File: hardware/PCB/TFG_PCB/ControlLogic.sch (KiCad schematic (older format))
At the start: 2 parts, among them J31 Raspberry_Pi_2_3, U7 CD74HC4067M

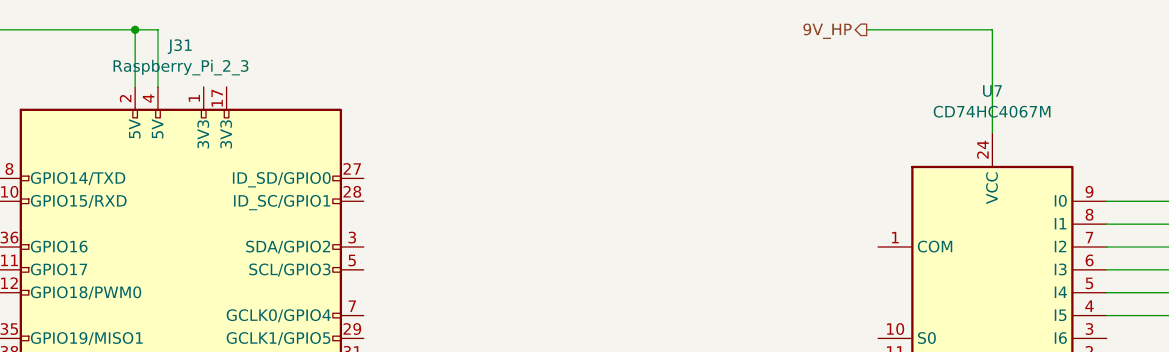
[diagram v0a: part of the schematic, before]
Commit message: added footprints
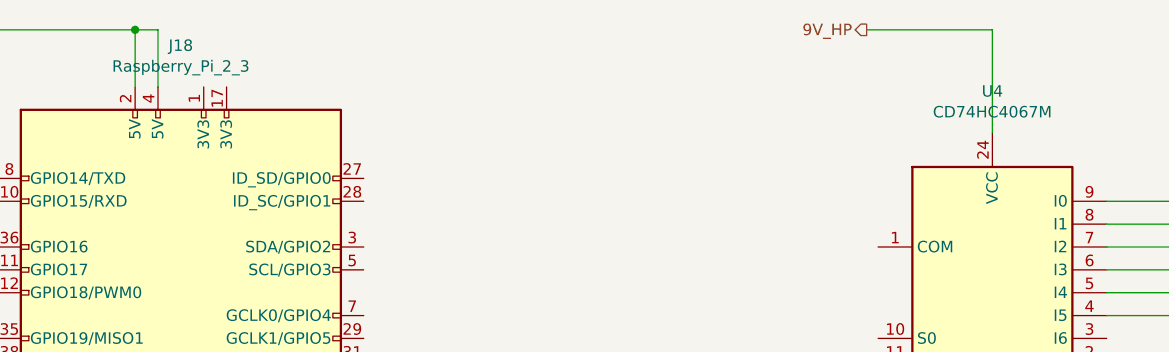
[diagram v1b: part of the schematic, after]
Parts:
- renumbered J31 to J18, U7 to U4
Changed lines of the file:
@@
 $EndDescr
 $Comp
-L Connector:Raspberry_Pi_2_3 J31
+L Connector:Raspberry_Pi_2_3 J18
 U 1 1 5E97206E
 P 3700 3450
-F 0 "J31" H 3700 4931 50  0000 C CNN
+F 0 "J18" H 3700 4931 50  0000 C CNN
 F 1 "Raspberry_Pi_2_3" H 3700 4840 50  0000 C CNN
 F 2 "" H 3700 3450 50  0001 C CNN
@@
 Connection ~ 3500 1900
 $Comp
-L 74xx:CD74HC4067M U7
+L 74xx:CD74HC4067M U4
 U 1 1 5E9A928D
 P 7250 3350
-F 0 "U7" H 7250 4531 50  0000 C CNN
+F 0 "U4" H 7250 4531 50  0000 C CNN
 F 1 "CD74HC4067M" H 7250 4440 50  0000 C CNN
 F 2 "Package_SO:SOIC-24W_7.5x15.4mm_P1.27mm" H 8150 2350 50  0001 C CIN
@@
 	3400 4850 3500 4850
 $Comp
-L power:GND #PWR0141
+L power:GND #PWR041
 U 1 1 5E9AD34B
 P 3650 4850
-F 0 "#PWR0141" H 3650 4600 50  0001 C CNN
+F 0 "#PWR041" H 3650 4600 50  0001 C CNN
 F 1 "GND" H 3655 4677 50  0000 C CNN
 F 2 "" H 3650 4850 50  0001 C CNN

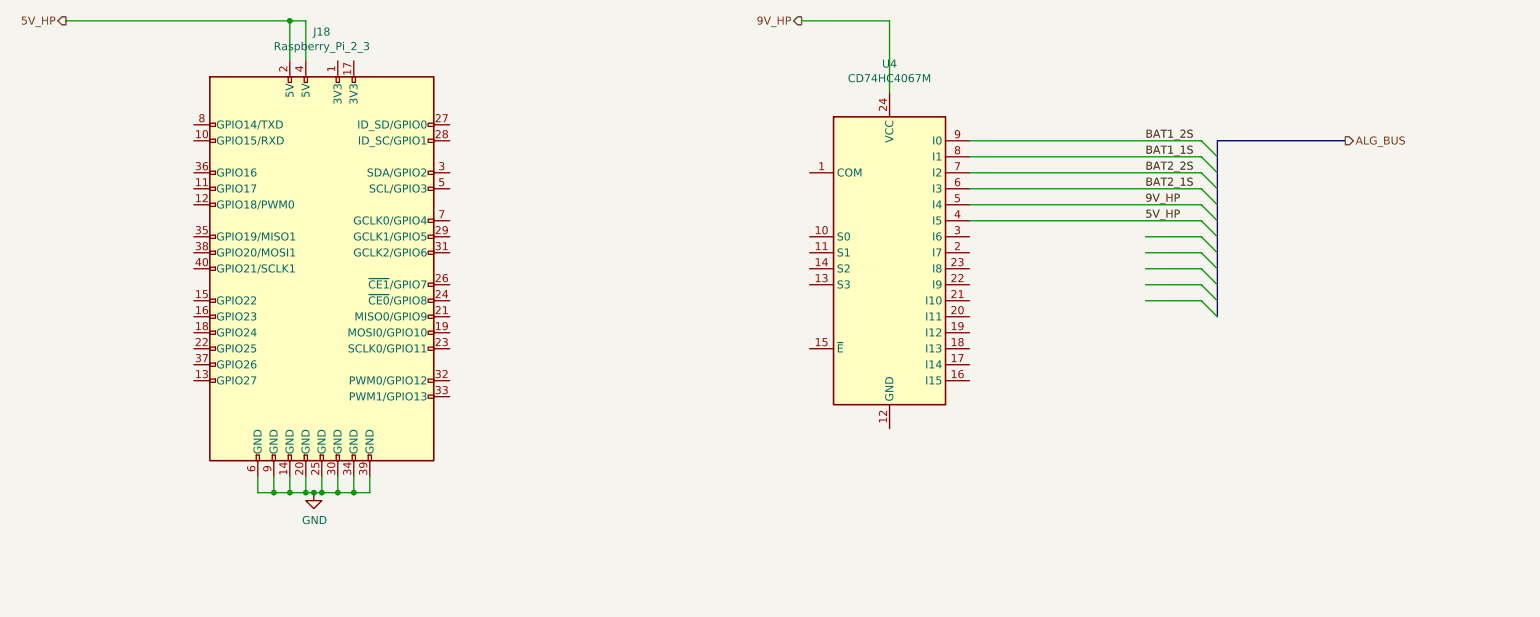
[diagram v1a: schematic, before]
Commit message: netlist and Motor Control sheet
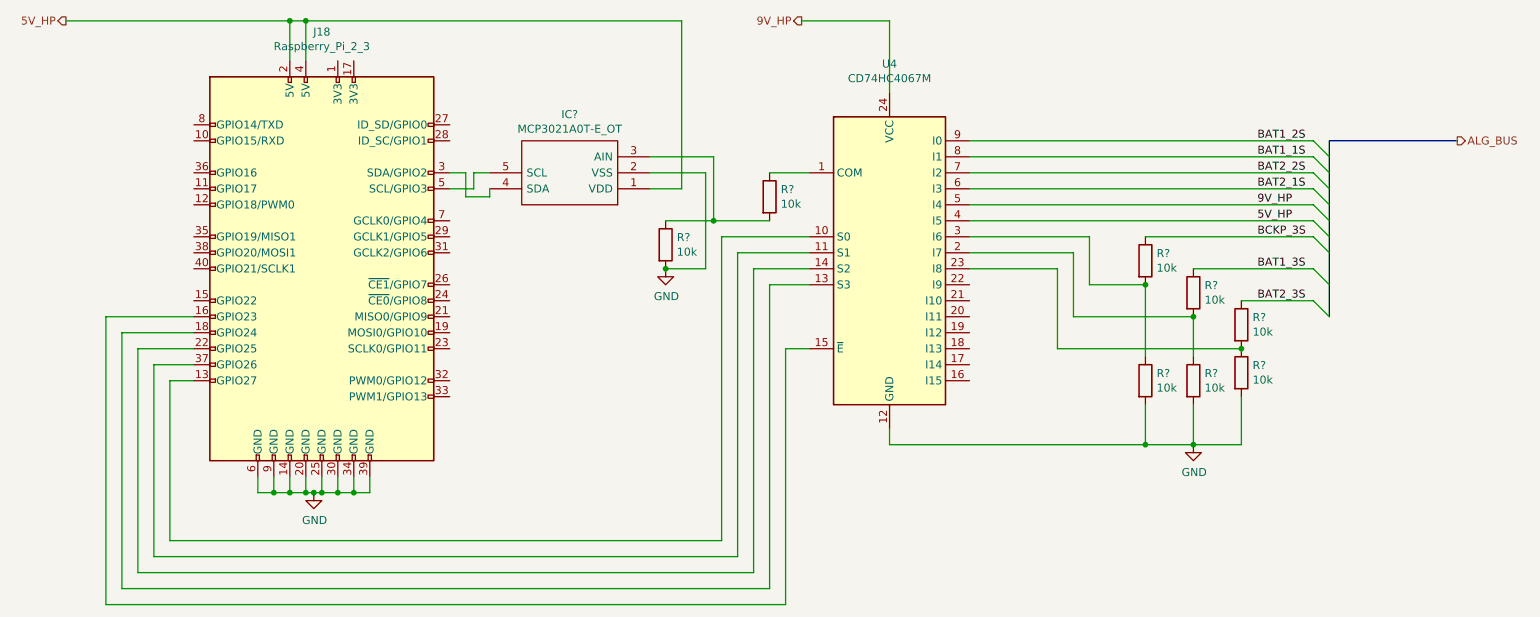
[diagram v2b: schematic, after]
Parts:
- added IC?: MCP3021A0T-E_OT, SOT95P280X145-5N, symbol SamacSys_Parts:MCP3021A0T-E_OT
- added R? (x8): 10k, symbol Device:R
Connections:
- net labels added: BAT1_3S, BAT2_3S, BCKP_3S
- wire segments 33 -> 92

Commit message: Updated netlist and footprints
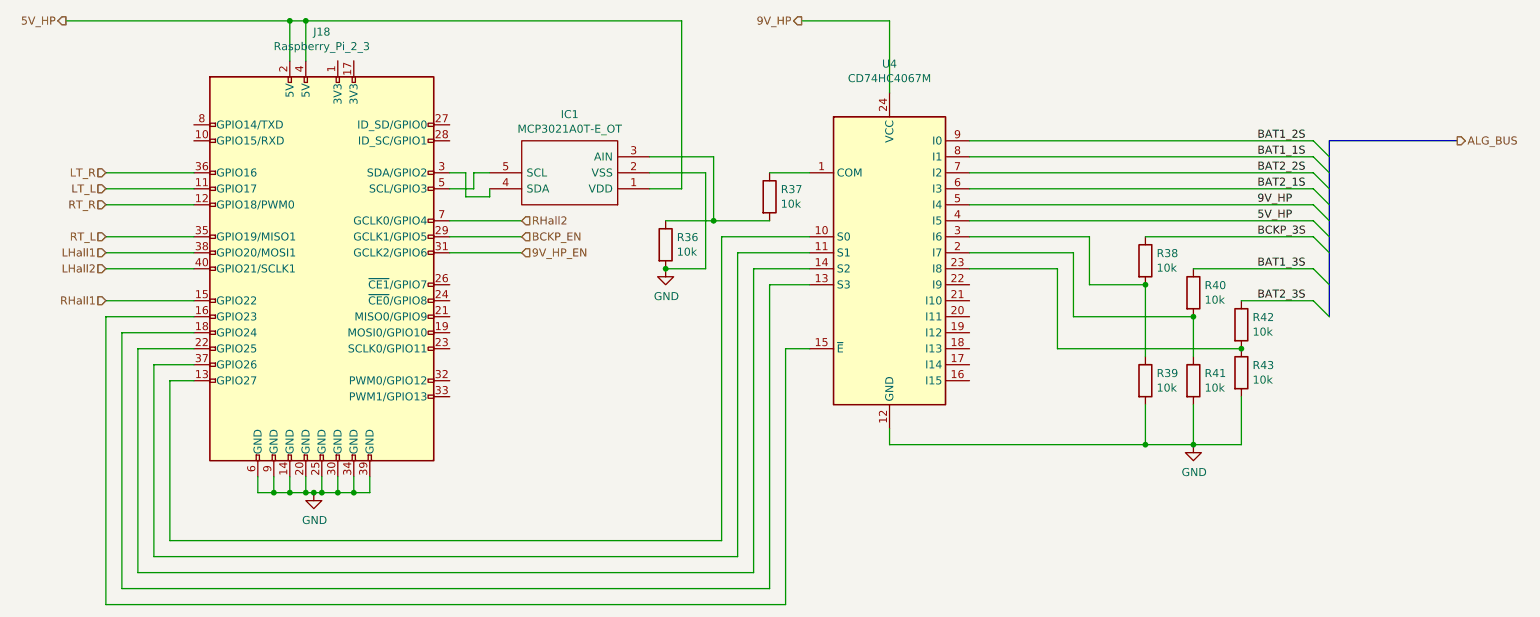
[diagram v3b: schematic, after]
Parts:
- J18: footprint (none) -> Connector_PinSocket_2.54mm:PinSocket_2x20_P2.54mm_Vertical
- R36, R37, R38, R39, R40, R41, R42, R43: renamed from R?; footprint (none) -> Resistor_SMD:R_0805_2012Metric_Pad1.15x1.40mm_HandSolder
- gave numbers to parts that had none: 1
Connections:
- net LT_L: now reaches J18.11 (GPIO17)
- net RT_R: now reaches J18.12 (GPIO18/PWM0)
- net RHall1: now reaches J18.15 (GPIO22)
- net BCKP_EN: now reaches J18.29 (GCLK1/GPIO5)
- net 9V_HP_EN: now reaches J18.31 (GCLK2/GPIO6)
- net RT_L: now reaches J18.35 (GPIO19/MISO1)
- net LT_R: now reaches J18.36 (GPIO16)
- net LHall1: now reaches J18.38 (GPIO20/MOSI1)
- net LHall2: now reaches J18.40 (GPIO21/SCLK1)
- net RHall2: now reaches J18.7 (GCLK0/GPIO4)
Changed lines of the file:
@@
 $Descr A4 11693 8268
 encoding utf-8
-Sheet 3 3
+Sheet 4 4
 Title ""
 Date ""
@@
 F 0 "J18" H 3700 4931 50  0000 C CNN
 F 1 "Raspberry_Pi_2_3" H 3700 4840 50  0000 C CNN
-F 2 "" H 3700 3450 50  0001 C CNN
+F 2 "Connector_PinSocket_2.54mm:PinSocket_2x20_P2.54mm_Vertical" H 3700 3450 50  0001 C CNN
 F 3 "https://www.raspberrypi.org/documentation/hardware/raspberrypi/schematics/rpi_SCH_3bplus_1p0_reduced.pdf" H 3700 3450 50  0001 C CNN
 	1    3700 3450
@@
 	7750 3150 9900 3150
 $Comp
-L Device:R R?
+L Device:R R38
 U 1 1 5E6201A7
 P 8850 3400
-F 0 "R?" H 8920 3446 50  0000 L CNN
+F 0 "R38" H 8920 3446 50  0000 L CNN
 F 1 "10k" H 8920 3355 50  0000 L CNN
-F 2 "" V 8780 3400 50  0001 C CNN
+F 2 "Resistor_SMD:R_0805_2012Metric_Pad1.15x1.40mm_HandSolder" V 8780 3400 50  0001 C CNN
 F 3 "~" H 8850 3400 50  0001 C CNN
 	1    8850 3400
@@
 $EndComp
 $Comp
-L Device:R R?
+L Device:R R42
 U 1 1 5E621BC0
 P 9450 3800
-F 0 "R?" H 9520 3846 50  0000 L CNN
+F 0 "R42" H 9520 3846 50  0000 L CNN
 F 1 "10k" H 9520 3755 50  0000 L CNN
-F 2 "" V 9380 3800 50  0001 C CNN
+F 2 "Resistor_SMD:R_0805_2012Metric_Pad1.15x1.40mm_HandSolder" V 9380 3800 50  0001 C CNN
 F 3 "~" H 9450 3800 50  0001 C CNN
 	1    9450 3800
@@
 $EndComp
 $Comp
-L Device:R R?
+L Device:R R43
 U 1 1 5E623E34
 P 9450 4100
-F 0 "R?" H 9520 4146 50  0000 L CNN
+F 0 "R43" H 9520 4146 50  0000 L CNN
 F 1 "10k" H 9520 4055 50  0000 L CNN
-F 2 "" V 9380 4100 50  0001 C CNN
+F 2 "Resistor_SMD:R_0805_2012Metric_Pad1.15x1.40mm_HandSolder" V 9380 4100 50  0001 C CNN
 F 3 "~" H 9450 4100 50  0001 C CNN
 	1    9450 4100
@@
 $EndComp
 $Comp
-L Device:R R?
+L Device:R R40
 U 1 1 5E624522
 P 9150 3600
-F 0 "R?" H 9220 3646 50  0000 L CNN
+F 0 "R40" H 9220 3646 50  0000 L CNN
 F 1 "10k" H 9220 3555 50  0000 L CNN
-F 2 "" V 9080 3600 50  0001 C CNN
+F 2 "Resistor_SMD:R_0805_2012Metric_Pad1.15x1.40mm_HandSolder" V 9080 3600 50  0001 C CNN
 F 3 "~" H 9150 3600 50  0001 C CNN
 	1    9150 3600
@@
 $EndComp
 $Comp
-L Device:R R?
+L Device:R R41
 U 1 1 5E62517F
 P 9150 4150
-F 0 "R?" H 9220 4196 50  0000 L CNN
+F 0 "R41" H 9220 4196 50  0000 L CNN
 F 1 "10k" H 9220 4105 50  0000 L CNN
-F 2 "" V 9080 4150 50  0001 C CNN
+F 2 "Resistor_SMD:R_0805_2012Metric_Pad1.15x1.40mm_HandSolder" V 9080 4150 50  0001 C CNN
 F 3 "~" H 9150 4150 50  0001 C CNN
 	1    9150 4150
@@
 $EndComp
 $Comp
-L Device:R R?
+L Device:R R39
 U 1 1 5E6260BB
 P 8850 4150
-F 0 "R?" H 8920 4196 50  0000 L CNN
+F 0 "R39" H 8920 4196 50  0000 L CNN
 F 1 "10k" H 8920 4105 50  0000 L CNN
-F 2 "" V 8780 4150 50  0001 C CNN
+F 2 "Resistor_SMD:R_0805_2012Metric_Pad1.15x1.40mm_HandSolder" V 8780 4150 50  0001 C CNN
 F 3 "~" H 8850 4150 50  0001 C CNN
 	1    8850 4150
@@
 	9450 3650 9900 3650
 $Comp
-L power:GND #PWR?
+L power:GND #PWR0112
 U 1 1 5E6277F8
 P 9150 4550
-F 0 "#PWR?" H 9150 4300 50  0001 C CNN
+F 0 "#PWR0112" H 9150 4300 50  0001 C CNN
 F 1 "GND" H 9155 4377 50  0000 C CNN
 F 2 "" H 9150 4550 50  0001 C CNN
@@
 	6600 3950 6750 3950
 $Comp
-L SamacSys_Parts:MCP3021A0T-E_OT IC?
+L SamacSys_Parts:MCP3021A0T-E_OT IC1
 U 1 1 5E64EE7F
 P 5750 2950
-F 0 "IC?" H 6250 2485 50  0000 C CNN
+F 0 "IC1" H 6250 2485 50  0000 C CNN
 F 1 "MCP3021A0T-E_OT" H 6250 2576 50  0000 C CNN
 F 2 "SOT95P280X145-5N" H 6600 3050 50  0001 L CNN
@@
 $EndComp
 $Comp
-L Device:R R?
+L Device:R R37
 U 1 1 5E65D601
 P 6500 3000
-F 0 "R?" H 6570 3046 50  0000 L CNN
+F 0 "R37" H 6570 3046 50  0000 L CNN
 F 1 "10k" H 6570 2955 50  0000 L CNN
-F 2 "" V 6430 3000 50  0001 C CNN
+F 2 "Resistor_SMD:R_0805_2012Metric_Pad1.15x1.40mm_HandSolder" V 6430 3000 50  0001 C CNN
 F 3 "~" H 6500 3000 50  0001 C CNN
 	1    6500 3000
@@
 $EndComp
 $Comp
-L Device:R R?
+L Device:R R36
 U 1 1 5E65FE45
 P 5850 3300
-F 0 "R?" H 5920 3346 50  0000 L CNN
+F 0 "R36" H 5920 3346 50  0000 L CNN
 F 1 "10k" H 5920 3255 50  0000 L CNN
-F 2 "" V 5780 3300 50  0001 C CNN
+F 2 "Resistor_SMD:R_0805_2012Metric_Pad1.15x1.40mm_HandSolder" V 5780 3300 50  0001 C CNN
 F 3 "~" H 5850 3300 50  0001 C CNN
 	1    5850 3300
@@
 	5850 3150 6150 3150
 $Comp
-L power:GND #PWR?
+L power:GND #PWR0113
 U 1 1 5E6630D9
 P 5850 3450
-F 0 "#PWR?" H 5850 3200 50  0001 C CNN
+F 0 "#PWR0113" H 5850 3200 50  0001 C CNN
 F 1 "GND" H 5855 3277 50  0000 C CNN
 F 2 "" H 5850 3450 50  0001 C CNN
@@
 Wire Wire Line
 	4650 2850 4750 2850
+Text HLabel 2350 2850 0    50   Input ~ 0
+LT_R
+Text HLabel 2350 2950 0    50   Input ~ 0
+LT_L
+Text HLabel 2350 3050 0    50   Input ~ 0
+RT_R
+Text HLabel 2350 3250 0    50   Input ~ 0
+RT_L
+Wire Wire Line
+	2350 2850 2900 2850
+Wire Wire Line
+	2900 2950 2350 2950
+Wire Wire Line
+	2350 3050 2900 3050
+Wire Wire Line
+	2900 3250 2350 3250
+Text HLabel 2350 3350 0    50   Input ~ 0
+LHall1
+Text HLabel 2350 3450 0    50   Input ~ 0
+LHall2
+Text HLabel 2350 3650 0    50   Input ~ 0
+RHall1
+Wire Wire Line
+	2350 3350 2900 3350
+Wire Wire Line
+	2900 3450 2350 3450
+Wire Wire Line
+	2350 3650 2900 3650
+Text HLabel 4950 3150 2    50   Input ~ 0
+RHall2
+Wire Wire Line
+	4950 3150 4500 3150
+Text HLabel 4950 3250 2    50   Input ~ 0
+BCKP_EN
+Text HLabel 4950 3350 2    50   Input ~ 0
+9V_HP_EN
+Wire Wire Line
+	4950 3350 4500 3350
+Wire Wire Line
+	4500 3250 4950 3250
 Wire Bus Line
 	10000 2650 10000 3750
